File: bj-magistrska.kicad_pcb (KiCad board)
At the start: 4 copper layers, 74.8 x 53.7 mm, 103 parts, among them J1 Screw_Terminal_01x02, J2 Conn_01x02, J3 Screw_Terminal_01x02, J4 Conn_01x04, J5 Conn_01x04, J6 Conn_01x03, Q1 DMTH10H009LPSQ-13, U1 TSV732IS, U10 MCP1501-33xSN, U2 74LVC1G17, U3 TSV732IS, U4 NUCLEO144-H743ZI, U6 INA240A2D, U8 ER_OLEDM0.91_1x-I2C, U9 MCP96xx01x-x-MX

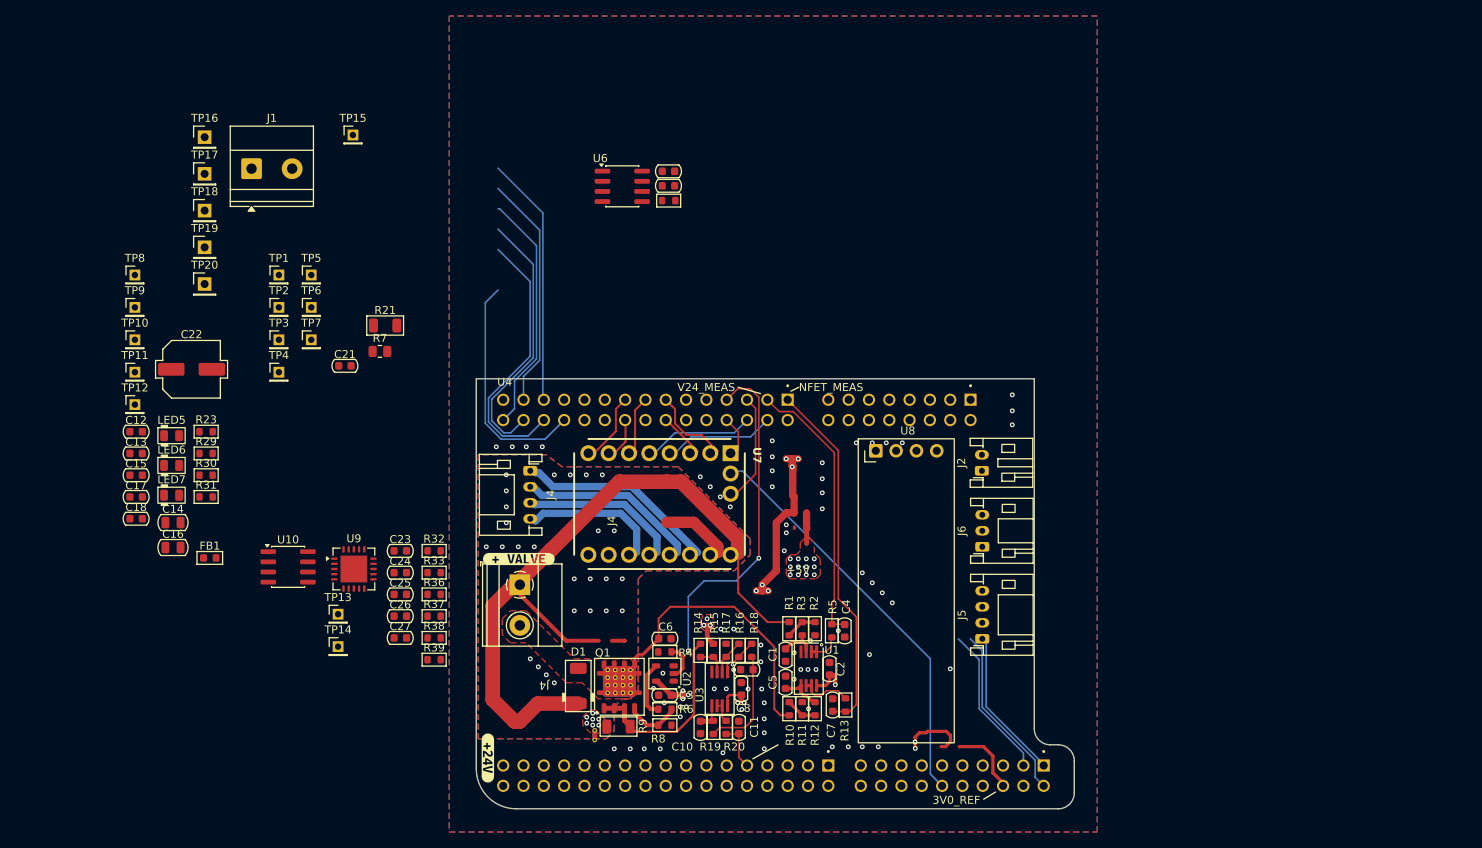
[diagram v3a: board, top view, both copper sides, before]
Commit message: Done some work on the PCB. Will rip it up to see if there is a better wway to run current of the coil.
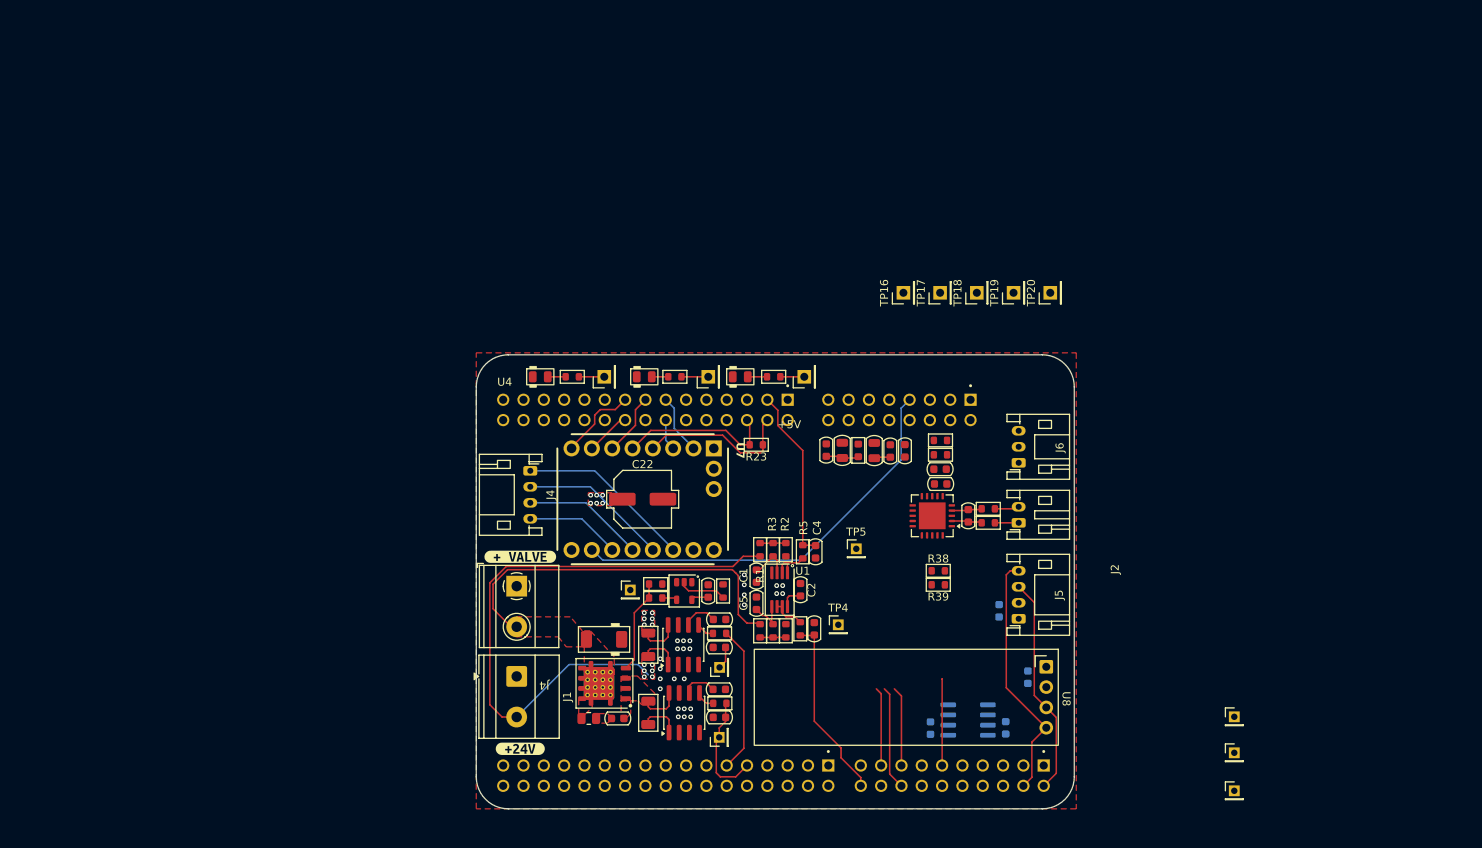
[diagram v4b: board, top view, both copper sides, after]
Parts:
- removed C10: 1n5, PCM_Capacitor_SMD_AKL:C_0603_1608Metric
- removed C6: 22n, PCM_Capacitor_SMD_AKL:C_0603_1608Metric
- removed C8, C9: 100n, PCM_Capacitor_SMD_AKL:C_0603_1608Metric
- removed NT1: NetTie_2, NetTie:NetTie-2_THT_Pad0.3mm
- removed R14: 100R, PCM_Resistor_SMD_AKL:R_0603_1608Metric
- removed R15, R19: 100k, PCM_Resistor_SMD_AKL:R_0603_1608Metric
- removed R16: 180k, PCM_Resistor_SMD_AKL:R_0603_1608Metric
- removed R17: 1k8, PCM_Resistor_SMD_AKL:R_0603_1608Metric
- removed R18: 220R, PCM_Resistor_SMD_AKL:R_0603_1608Metric
- removed TP11, TP15, TP6, TP7: TestPoint, Connector_PinHeader_2.00mm:PinHeader_1x01_P2.00mm_Vertical
- removed U3: TSV732IS, PCM_Package_SO_AKL:MSOP-8_3x3mm_P0.65mm
- added C28: 100n, PCM_Capacitor_SMD_AKL:C_0603_1608Metric, F.Cu at (112.2, 133.5)
- added U11: INA240A2D, Package_SO:SOIC-8_3.9x4.9mm_P1.27mm, F.Cu at (107.8, 136.4)
- C17, C18, C25, C26, U10: moved to B.Cu
- C21: value 0 -> ~
- R6: value 1k -> 100R
- R7: value R -> ~
- TP10, TP8, TP9: footprint Connector_PinHeader_2.00mm:PinHeader_1x01_P2.00mm_Vertical -> Connector_PinHeader_2.54mm:PinHeader_1x01_P2.54mm_Vertical
- U7: value ~ -> BTT TMC2209 V1.3
- moved TP12 142.9 mm to (176.6, 136.9)
- moved TP14 113.5 mm to (176.6, 146.2)
- moved TP13 113.4 mm to (176.6, 141.4)
- moved C18 111.8 mm to (148.0, 138.3), turned to 90 degrees
- moved TP20 105.7 mm to (153.6, 84.0), turned to 90 degrees
- moved C17 103.4 mm to (138.6, 138.4), turned to 90 degrees
- moved TP19 101.3 mm to (149.0, 84.0), turned to 90 degrees
- moved TP18 97.1 mm to (144.4, 84.0), turned to 90 degrees
- moved C13 96.1 mm to (135.4, 103.7), turned to -90 degrees
- moved C12 94.3 mm to (133.6, 103.7), turned to 90 degrees
- moved TP17 93.1 mm to (139.8, 84.0), turned to 90 degrees
- moved TP16 89.5 mm to (135.2, 84.0), turned to 90 degrees
- moved C14 88.1 mm to (131.6, 103.7), turned to 90 degrees
- moved U10 87.1 mm to (143.3, 137.4)
- moved C15 86.3 mm to (125.6, 103.6), turned to 90 degrees
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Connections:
- C22 pad 2: GNDPWR -> GND
- J1 pad 1: GNDPWR -> GND
- R9 pad 2: GNDPWR -> GND
- U7 pad 15: GNDPWR -> GND
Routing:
- net +5VD: track 75.0 -> 4.48 mm, vias 9 -> 0
- net +3V3: track 0.00 -> 52.3 mm
- net TMC2209_VREF: track 50.2 -> 0.00 mm
- net unconnected-(U4-РАЗ-PadCN9_1): track 45.0 -> 0.00 mm
- net /Nucleo-144/IO_PWM_CONTROL: track 48.3 -> 5.96 mm, vias 2 -> 0
- net unconnected-(U4-PF7-PadCN9_26): track 33.8 -> 0.00 mm
- net unconnected-(U4-PF9-PadCN9_28): track 33.2 -> 0.00 mm
- net I2C1_SDA: track 0.00 -> 31.4 mm
- net unconnected-(U4-PD0-PadCN9_25): track 31.3 -> 0.00 mm
- net unconnected-(U4-PG1-PadCN9_30): track 30.2 -> 0.00 mm
- net unconnected-(U4-PD1-PadCN9_27): track 29.4 -> 0.00 mm
- net unconnected-(U4-PF8-PadCN9_24): track 29.0 -> 0.00 mm
- net /Nucleo-144/ADC_VFET: track 0.00 -> 23.0 mm
- net /Nucleo-144/ADC_IFET_HS: track 0.00 -> 21.1 mm
- net unconnected-(U4-PB15-PadCN7_3): track 19.8 -> 0.00 mm
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- added copper zone on F.Cu, net +12V
- added copper zone on In2.Cu, net +12V
- added copper zone on F.Cu, net /Output_Analog/COIL_OUT
- added copper zone on F.Cu, net Net-(C21-Pad1)
- added copper zone on F.Cu, net Net-(U11-+)
- removed copper zone on In2.Cu, net +3V3
- removed copper zone on F.Cu, net +5VA
- removed copper zone on In2.Cu, net +5VA
- removed copper zone on B.Cu, net GND
- removed copper zone on B.Cu, net GNDPWR
- removed copper zone on F.Cu, net GNDPWR
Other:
- board size 74.8 x 53.7 mm -> 74.8 x 56.7 mm
- board text removed: "3V0_REF"
- board text removed: "NFET_MEAS"
- board text removed: "V24_MEAS"
